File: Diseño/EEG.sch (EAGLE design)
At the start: 40 parts, among them IC1 REF2033AIDDCT, IC2 MCP73831T-2ACI_OT, IC3 LP38692MP-3.3_NOPB, J1 USB3500-30-A-KIT, J2 SJ3-35083A-TR

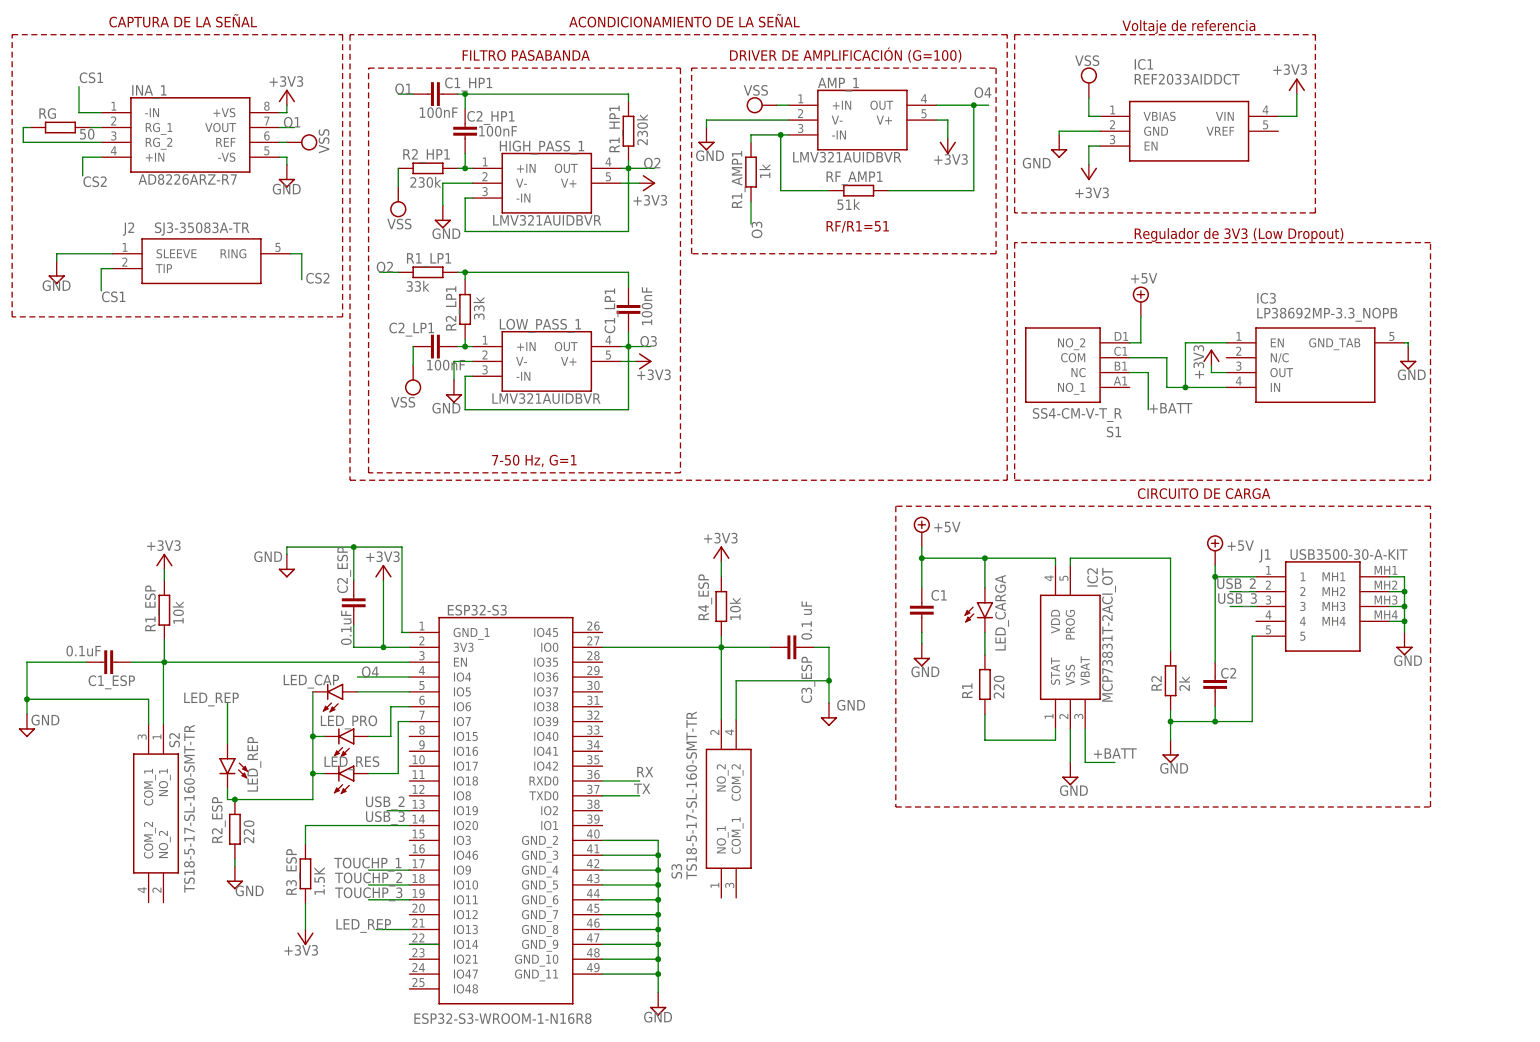
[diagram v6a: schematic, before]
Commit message: Se adelantó la PCB separando los componentes por secciones de potencia, analógica y digital
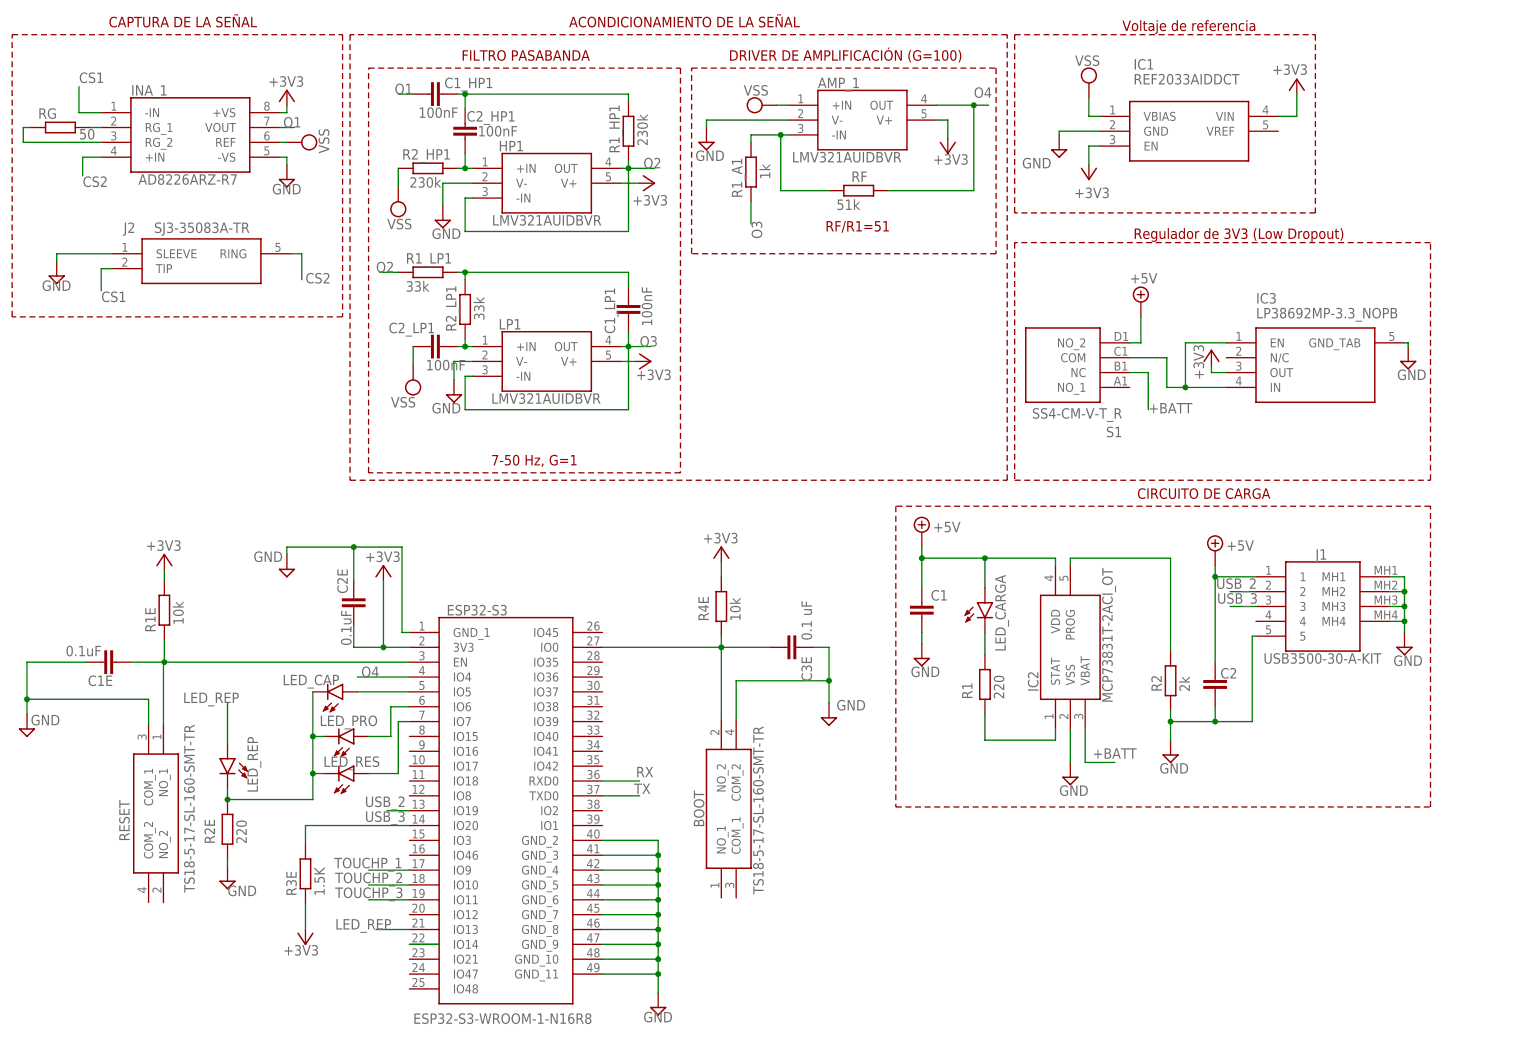
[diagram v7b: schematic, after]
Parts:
- removed R2_ESP: 220, rcl:R-EU_R0805
- added R2E: 220, rcl:R-EU_R0805
- renumbered C1_ESP to C1E, C2_ESP to C2E, C3_ESP to C3E, HIGH_PASS_1 to HP1, LOW_PASS_1 to LP1, R1_AMP1 to R1_A1, R1_ESP to R1E, R3_ESP to R3E, R4_ESP to R4E, RF_AMP1 to RF, S2 to RESET, S3 to BOOT
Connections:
- net GND: now also R2E.1; no longer R2_ESP.1
- net N$15: now also R2E.2; no longer R2_ESP.2

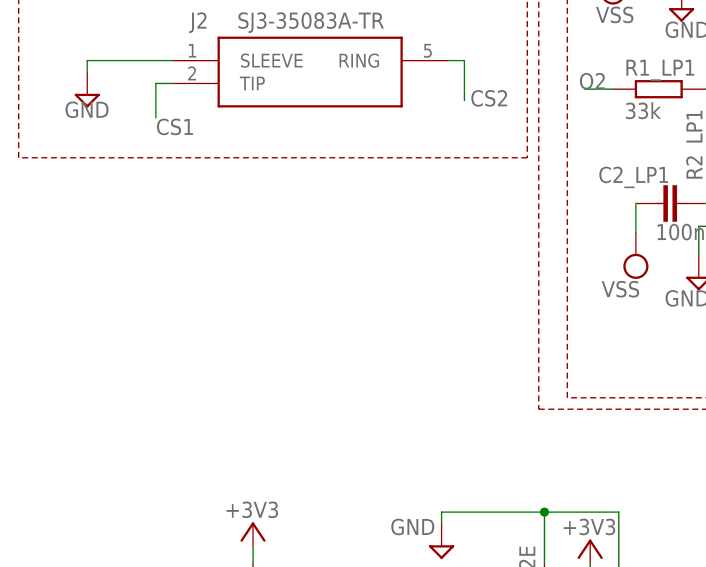
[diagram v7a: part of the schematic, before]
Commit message: añadí el conector de la bateria
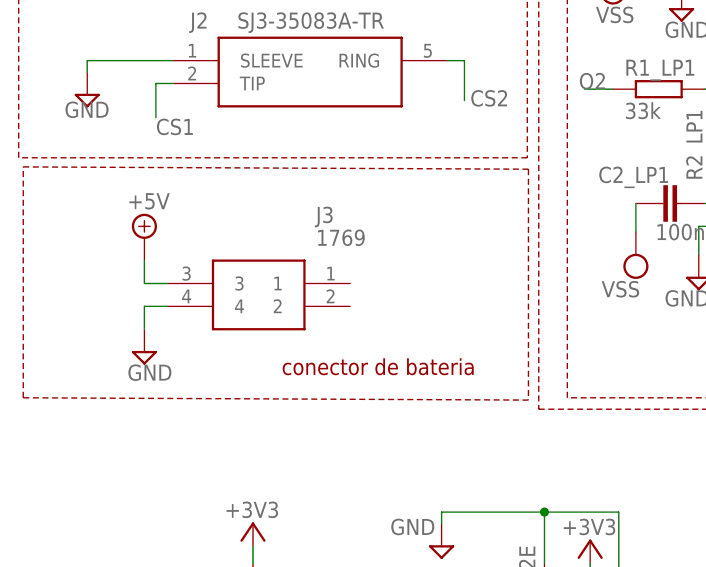
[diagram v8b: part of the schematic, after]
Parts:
- added J3: 1769, 1769 (1):1769
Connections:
- net +5V: now also J3.3
- net GND: now also J3.4
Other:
- note added: "conector de bateria"
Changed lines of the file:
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@@
 <part name="LED_RES" library="led" library_urn="urn:adsk.eagle:library:259" deviceset="LED" device="CHIPLED_0805" package3d_urn="urn:adsk.eagle:package:15821/2"/>
 <part name="R2E" library="rcl" library_urn="urn:adsk.eagle:library:334" deviceset="R-EU_" device="R0805" package3d_urn="urn:adsk.eagle:package:23553/2" value="220"/>
+<part name="J3" library="1769 (1)" deviceset="1769" device=""/>
+<part name="SUPPLY18" library="supply2" library_urn="urn:adsk.eagle:library:372" deviceset="+5V" device=""/>
+<part name="SUPPLY19" library="supply2" library_urn="urn:adsk.eagle:library:372" deviceset="GND" device=""/>
 </parts>
 <sheets>
@@
 <wire x1="243.84" y1="143.51" x2="172.72" y2="143.51" width="0.1524" layer="94" style="shortdash"/>
 <text x="193.04" y="144.145" size="1.778" layer="94">Regulador de 3V3 (Low Dropout)</text>
+<wire x1="1.778" y1="129.794" x2="57.912" y2="129.54" width="0.1524" layer="94" style="shortdash"/>
+<wire x1="57.912" y1="129.54" x2="57.912" y2="103.886" width="0.1524" layer="94" style="shortdash"/>
+<wire x1="57.912" y1="103.886" x2="1.778" y2="104.14" width="0.1524" layer="94" style="shortdash"/>
+<wire x1="1.778" y1="104.14" x2="1.778" y2="129.794" width="0.1524" layer="94" style="shortdash"/>
+<text x="30.48" y="106.68" size="1.778" layer="94">conector de bateria</text>
 </plain>
 <instances>
@@
 <attribute name="NAME" x="35.9664" y="40.64" size="1.778" layer="95" rot="R90"/>
 <attribute name="VALUE" x="41.402" y="40.64" size="1.778" layer="96" rot="R90"/>
+</instance>
+<instance part="J3" gate="G$1" x="17.78" y="116.84" smashed="yes">
+<attribute name="NAME" x="34.29" y="124.46" size="1.778" layer="95" align="center-left"/>
+<attribute name="VALUE" x="34.29" y="121.92" size="1.778" layer="96" align="center-left"/>
+</instance>
+<instance part="SUPPLY18" gate="+5V" x="15.24" y="121.92" smashed="yes">
+<attribute name="VALUE" x="13.335" y="125.095" size="1.778" layer="96"/>
+</instance>
+<instance part="SUPPLY19" gate="GND" x="15.24" y="109.22" smashed="yes">
+<attribute name="VALUE" x="13.335" y="106.045" size="1.778" layer="96"/>
 </instance>
 </instances>
@@
 <wire x1="38.1" y1="36.83" x2="38.1" y2="38.1" width="0.1524" layer="91"/>
 </segment>
+<segment>
+<pinref part="SUPPLY19" gate="GND" pin="GND"/>
+<wire x1="15.24" y1="111.76" x2="15.24" y2="114.3" width="0.1524" layer="91"/>
+<pinref part="J3" gate="G$1" pin="4"/>
+<wire x1="15.24" y1="114.3" x2="17.78" y2="114.3" width="0.1524" layer="91"/>
+</segment>
 </net>
 <net name="N$3" class="0">
@@
 <junction x="207.01" y="86.36"/>
 </segment>
-</net>
+<segment>
+<pinref part="SUPPLY18" gate="+5V" pin="+5V"/>
+<pinref part="J3" gate="G$1" pin="3"/>
+<wire x1="15.24" y1="119.38" x2="15.24" y2="116.84" width="0.1524" layer="91"/>
+<wire x1="15.24" y1="116.84" x2="17.78" y2="116.84" width="0.1524" layer="91"/>
+</segment>
+</net>
